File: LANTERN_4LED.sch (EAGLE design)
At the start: 6 parts

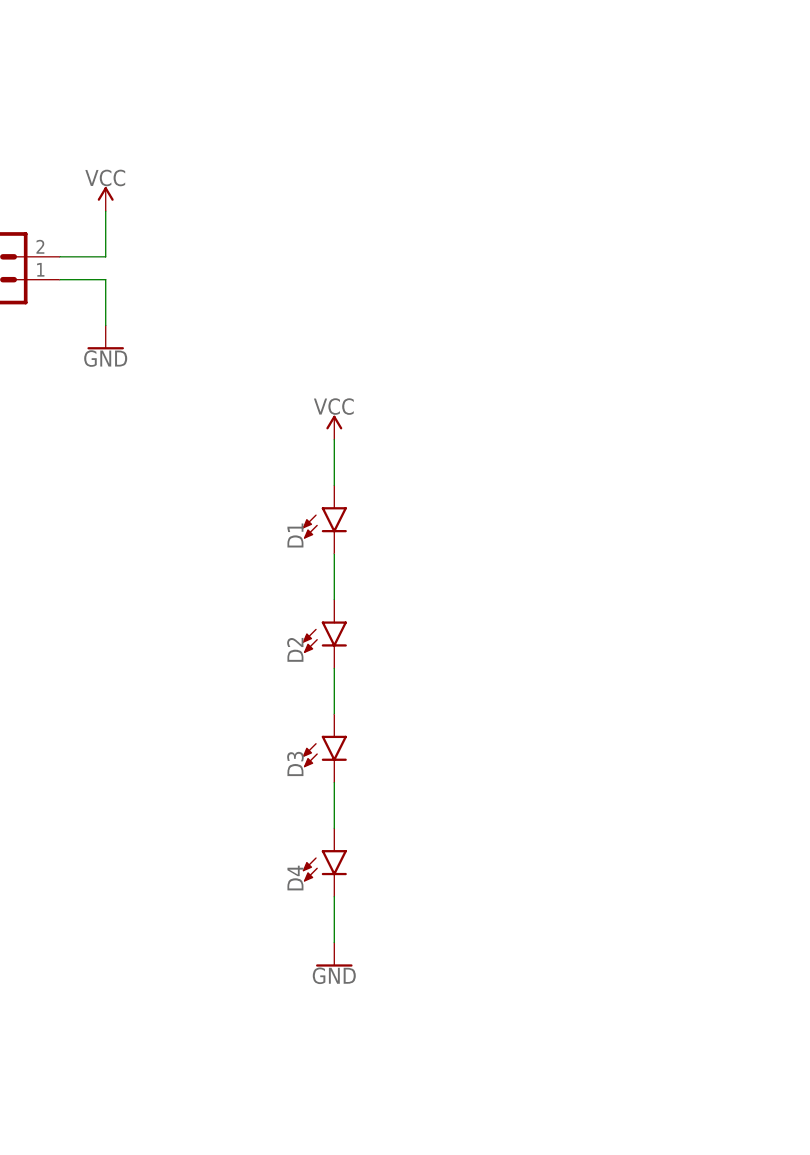
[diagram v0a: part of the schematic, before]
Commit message: Designed for 2 layer board
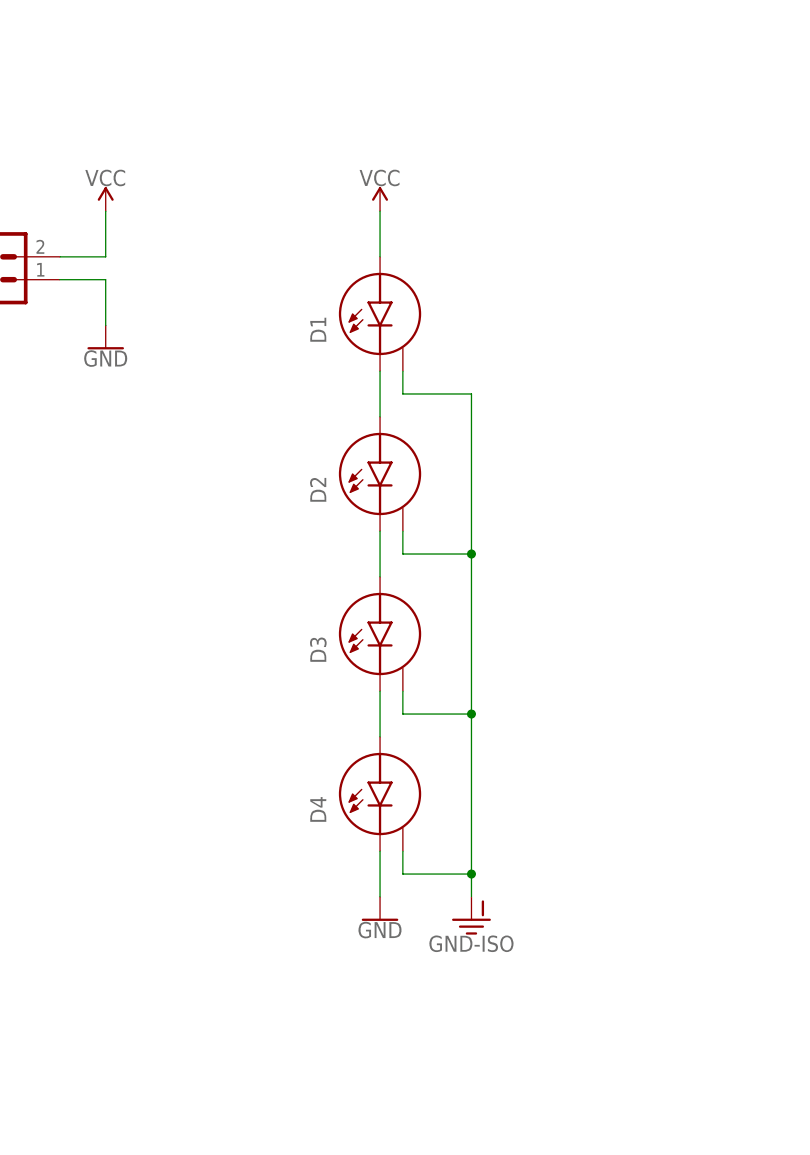
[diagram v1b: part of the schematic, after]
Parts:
- D1, D2, D3, D4: device my_library:LED1414_HC -> my_library:LED_H1414_H
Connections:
- new net GND-ISO: D1.H, D2.H, D3.H, D4.H
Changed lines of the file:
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@@
 </classes>
 <parts>
-<part name="D1" library="my_library" deviceset="LED" device="1414_HC"/>
-<part name="D2" library="my_library" deviceset="LED" device="1414_HC"/>
-<part name="D3" library="my_library" deviceset="LED" device="1414_HC"/>
-<part name="D4" library="my_library" deviceset="LED" device="1414_HC"/>
 <part name="GND1" library="SparkFun-PowerSymbols" deviceset="GND" device=""/>
 <part name="SUPPLY1" library="SparkFun-PowerSymbols" deviceset="VCC" device=""/>
@@
 <part name="GND2" library="SparkFun-PowerSymbols" deviceset="GND" device=""/>
 <part name="FRAME1" library="SparkFun-Aesthetics" deviceset="FRAME-LETTER" device="NO_PACKAGE"/>
+<part name="D1" library="my_library" deviceset="LED_H" device="1414_H"/>
+<part name="D2" library="my_library" deviceset="LED_H" device="1414_H"/>
+<part name="D3" library="my_library" deviceset="LED_H" device="1414_H"/>
+<part name="D4" library="my_library" deviceset="LED_H" device="1414_H"/>
+<part name="GND-ISO1" library="SparkFun-PowerSymbols" deviceset="GND-ISO" device=""/>
 </parts>
 <sheets>
@@
 </plain>
 <instances>
-<instance part="D1" gate="G$1" x="99.06" y="114.3"/>
-<instance part="D2" gate="G$1" x="99.06" y="101.6"/>
-<instance part="D3" gate="G$1" x="99.06" y="88.9"/>
-<instance part="D4" gate="G$1" x="99.06" y="76.2"/>
-<instance part="GND1" gate="1" x="99.06" y="63.5"/>
-<instance part="SUPPLY1" gate="G$1" x="99.06" y="121.92"/>
+<instance part="GND1" gate="1" x="104.14" y="68.58"/>
+<instance part="SUPPLY1" gate="G$1" x="104.14" y="147.32"/>
 <instance part="J1" gate="G$1" x="60.96" y="139.7"/>
 <instance part="SUPPLY2" gate="G$1" x="73.66" y="147.32"/>
@@
 <instance part="FRAME1" gate="G$1" x="0" y="0"/>
 <instance part="FRAME1" gate="V" x="147.32" y="0"/>
+<instance part="D1" gate="G$1" x="104.14" y="137.16"/>
+<instance part="D2" gate="G$1" x="104.14" y="119.38"/>
+<instance part="D3" gate="G$1" x="104.14" y="101.6"/>
+<instance part="D4" gate="G$1" x="104.14" y="83.82"/>
+<instance part="GND-ISO1" gate="G$1" x="114.3" y="68.58"/>
 </instances>
 <busses>
@@
 <net name="VCC" class="0">
 <segment>
-<pinref part="SUPPLY1" gate="G$1" pin="VCC"/>
-<pinref part="D1" gate="G$1" pin="A"/>
-<wire x1="99.06" y1="121.92" x2="99.06" y2="116.84" width="0.1524" layer="91"/>
-</segment>
-<segment>
 <pinref part="J1" gate="G$1" pin="2"/>
 <pinref part="SUPPLY2" gate="G$1" pin="VCC"/>
 <wire x1="68.58" y1="142.24" x2="73.66" y2="142.24" width="0.1524" layer="91"/>
 <wire x1="73.66" y1="142.24" x2="73.66" y2="147.32" width="0.1524" layer="91"/>
+</segment>
+<segment>
+<pinref part="SUPPLY1" gate="G$1" pin="VCC"/>
+<pinref part="D1" gate="G$1" pin="A"/>
+<wire x1="104.14" y1="147.32" x2="104.14" y2="142.24" width="0.1524" layer="91"/>
+</segment>
+</net>
+<net name="GND" class="0">
+<segment>
+<pinref part="J1" gate="G$1" pin="1"/>
+<pinref part="GND2" gate="1" pin="GND"/>
+<wire x1="68.58" y1="139.7" x2="73.66" y2="139.7" width="0.1524" layer="91"/>
+<wire x1="73.66" y1="139.7" x2="73.66" y2="134.62" width="0.1524" layer="91"/>
+</segment>
+<segment>
+<pinref part="D4" gate="G$1" pin="C"/>
+<pinref part="GND1" gate="1" pin="GND"/>
+<wire x1="104.14" y1="76.2" x2="104.14" y2="71.12" width="0.1524" layer="91"/>
 </segment>
 </net>
@@
 <pinref part="D1" gate="G$1" pin="C"/>
 <pinref part="D2" gate="G$1" pin="A"/>
-<wire x1="99.06" y1="109.22" x2="99.06" y2="104.14" width="0.1524" layer="91"/>
+<wire x1="104.14" y1="129.54" x2="104.14" y2="124.46" width="0.1524" layer="91"/>
 </segment>
 </net>
@@
 <pinref part="D2" gate="G$1" pin="C"/>
 <pinref part="D3" gate="G$1" pin="A"/>
-<wire x1="99.06" y1="96.52" x2="99.06" y2="91.44" width="0.1524" layer="91"/>
+<wire x1="104.14" y1="111.76" x2="104.14" y2="106.68" width="0.1524" layer="91"/>
 </segment>
 </net>
@@
 <pinref part="D3" gate="G$1" pin="C"/>
 <pinref part="D4" gate="G$1" pin="A"/>
-<wire x1="99.06" y1="83.82" x2="99.06" y2="78.74" width="0.1524" layer="91"/>
+<wire x1="104.14" y1="93.98" x2="104.14" y2="88.9" width="0.1524" layer="91"/>
 </segment>
 </net>
-<net name="GND" class="0">
+<net name="GND-ISO" class="0">
 <segment>
-<pinref part="D4" gate="G$1" pin="C"/>
-<pinref part="GND1" gate="1" pin="GND"/>
-<wire x1="99.06" y1="71.12" x2="99.06" y2="66.04" width="0.1524" layer="91"/>
-</segment>
-<segment>
-<pinref part="J1" gate="G$1" pin="1"/>
-<pinref part="GND2" gate="1" pin="GND"/>
-<wire x1="68.58" y1="139.7" x2="73.66" y2="139.7" width="0.1524" layer="91"/>
-<wire x1="73.66" y1="139.7" x2="73.66" y2="134.62" width="0.1524" layer="91"/>
+<pinref part="D4" gate="G$1" pin="H"/>
+<wire x1="106.68" y1="76.2" x2="106.68" y2="73.66" width="0.1524" layer="91"/>
+<pinref part="GND-ISO1" gate="G$1" pin="GND-ISO"/>
+<wire x1="106.68" y1="73.66" x2="114.3" y2="73.66" width="0.1524" layer="91"/>
+<wire x1="114.3" y1="73.66" x2="114.3" y2="71.12" width="0.1524" layer="91"/>
+<pinref part="D3" gate="G$1" pin="H"/>
+<wire x1="106.68" y1="93.98" x2="106.68" y2="91.44" width="0.1524" layer="91"/>
+<wire x1="106.68" y1="91.44" x2="114.3" y2="91.44" width="0.1524" layer="91"/>
+<wire x1="114.3" y1="91.44" x2="114.3" y2="73.66" width="0.1524" layer="91"/>
+<pinref part="D2" gate="G$1" pin="H"/>
+<wire x1="106.68" y1="111.76" x2="106.68" y2="109.22" width="0.1524" layer="91"/>
+<wire x1="106.68" y1="109.22" x2="114.3" y2="109.22" width="0.1524" layer="91"/>
+<wire x1="114.3" y1="109.22" x2="114.3" y2="91.44" width="0.1524" layer="91"/>
+<pinref part="D1" gate="G$1" pin="H"/>
+<wire x1="106.68" y1="129.54" x2="106.68" y2="127" width="0.1524" layer="91"/>
+<wire x1="106.68" y1="127" x2="114.3" y2="127" width="0.1524" layer="91"/>
+<wire x1="114.3" y1="127" x2="114.3" y2="109.22" width="0.1524" layer="91"/>
+<junction x="114.3" y="109.22"/>
+<junction x="114.3" y="91.44"/>
+<junction x="114.3" y="73.66"/>
 </segment>
 </net>

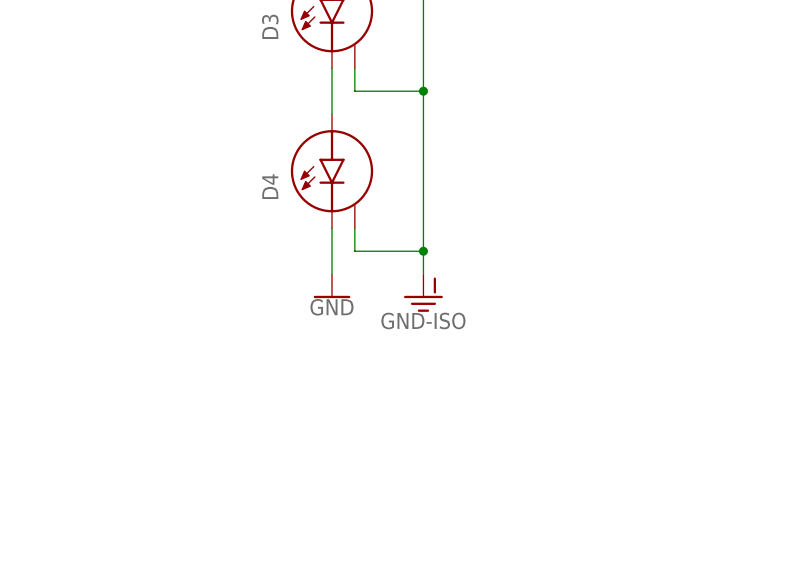
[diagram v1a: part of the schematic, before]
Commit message: Tied the heatsinks to ground.
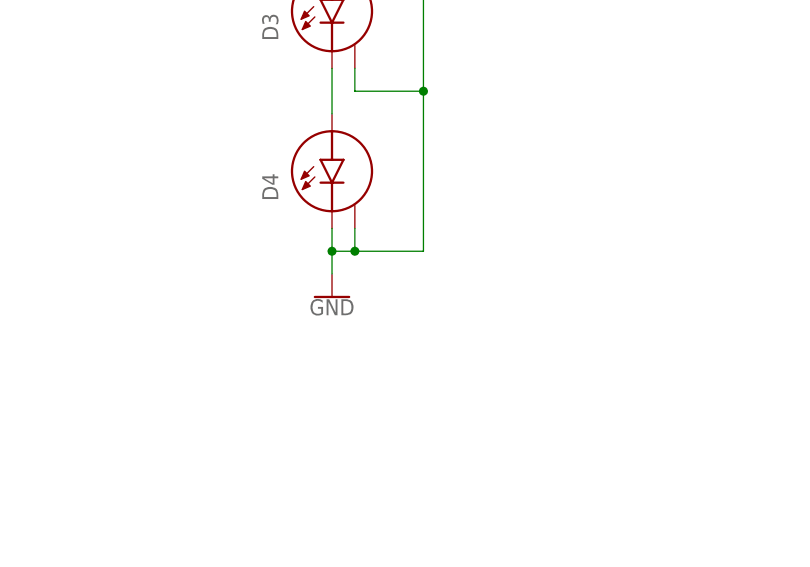
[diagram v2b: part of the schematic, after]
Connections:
- removed net GND-ISO: D1.H, D2.H, D3.H, D4.H
- net GND: now also D1.H, D2.H, D3.H, D4.H
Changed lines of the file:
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@@
 <part name="D3" library="my_library" deviceset="LED_H" device="1414_H"/>
 <part name="D4" library="my_library" deviceset="LED_H" device="1414_H"/>
-<part name="GND-ISO1" library="SparkFun-PowerSymbols" deviceset="GND-ISO" device=""/>
 </parts>
 <sheets>
@@
 <instance part="D3" gate="G$1" x="104.14" y="101.6"/>
 <instance part="D4" gate="G$1" x="104.14" y="83.82"/>
-<instance part="GND-ISO1" gate="G$1" x="114.3" y="68.58"/>
 </instances>
 <busses>
@@
 <pinref part="D4" gate="G$1" pin="C"/>
 <pinref part="GND1" gate="1" pin="GND"/>
-<wire x1="104.14" y1="76.2" x2="104.14" y2="71.12" width="0.1524" layer="91"/>
+<wire x1="104.14" y1="76.2" x2="104.14" y2="73.66" width="0.1524" layer="91"/>
+<pinref part="D3" gate="G$1" pin="H"/>
+<wire x1="104.14" y1="73.66" x2="104.14" y2="71.12" width="0.1524" layer="91"/>
+<wire x1="106.68" y1="93.98" x2="106.68" y2="91.44" width="0.1524" layer="91"/>
+<wire x1="106.68" y1="91.44" x2="114.3" y2="91.44" width="0.1524" layer="91"/>
+<pinref part="D2" gate="G$1" pin="H"/>
+<wire x1="106.68" y1="111.76" x2="106.68" y2="109.22" width="0.1524" layer="91"/>
+<wire x1="106.68" y1="109.22" x2="114.3" y2="109.22" width="0.1524" layer="91"/>
+<wire x1="114.3" y1="109.22" x2="114.3" y2="91.44" width="0.1524" layer="91"/>
+<pinref part="D1" gate="G$1" pin="H"/>
+<wire x1="106.68" y1="129.54" x2="106.68" y2="127" width="0.1524" layer="91"/>
+<wire x1="106.68" y1="127" x2="114.3" y2="127" width="0.1524" layer="91"/>
+<wire x1="114.3" y1="127" x2="114.3" y2="109.22" width="0.1524" layer="91"/>
+<junction x="114.3" y="109.22"/>
+<wire x1="114.3" y1="91.44" x2="114.3" y2="73.66" width="0.1524" layer="91"/>
+<wire x1="114.3" y1="73.66" x2="106.68" y2="73.66" width="0.1524" layer="91"/>
+<junction x="114.3" y="91.44"/>
+<pinref part="D4" gate="G$1" pin="H"/>
+<wire x1="106.68" y1="73.66" x2="104.14" y2="73.66" width="0.1524" layer="91"/>
+<wire x1="106.68" y1="76.2" x2="106.68" y2="73.66" width="0.1524" layer="91"/>
+<junction x="106.68" y="73.66"/>
+<junction x="104.14" y="73.66"/>
 </segment>
 </net>
@@
 </segment>
 </net>
-<net name="GND-ISO" class="0">
-<segment>
-<pinref part="D4" gate="G$1" pin="H"/>
-<wire x1="106.68" y1="76.2" x2="106.68" y2="73.66" width="0.1524" layer="91"/>
-<pinref part="GND-ISO1" gate="G$1" pin="GND-ISO"/>
-<wire x1="106.68" y1="73.66" x2="114.3" y2="73.66" width="0.1524" layer="91"/>
-<wire x1="114.3" y1="73.66" x2="114.3" y2="71.12" width="0.1524" layer="91"/>
-<pinref part="D3" gate="G$1" pin="H"/>
-<wire x1="106.68" y1="93.98" x2="106.68" y2="91.44" width="0.1524" layer="91"/>
-<wire x1="106.68" y1="91.44" x2="114.3" y2="91.44" width="0.1524" layer="91"/>
-<wire x1="114.3" y1="91.44" x2="114.3" y2="73.66" width="0.1524" layer="91"/>
-<pinref part="D2" gate="G$1" pin="H"/>
-<wire x1="106.68" y1="111.76" x2="106.68" y2="109.22" width="0.1524" layer="91"/>
-<wire x1="106.68" y1="109.22" x2="114.3" y2="109.22" width="0.1524" layer="91"/>
-<wire x1="114.3" y1="109.22" x2="114.3" y2="91.44" width="0.1524" layer="91"/>
-<pinref part="D1" gate="G$1" pin="H"/>
-<wire x1="106.68" y1="129.54" x2="106.68" y2="127" width="0.1524" layer="91"/>
-<wire x1="106.68" y1="127" x2="114.3" y2="127" width="0.1524" layer="91"/>
-<wire x1="114.3" y1="127" x2="114.3" y2="109.22" width="0.1524" layer="91"/>
-<junction x="114.3" y="109.22"/>
-<junction x="114.3" y="91.44"/>
-<junction x="114.3" y="73.66"/>
-</segment>
-</net>
